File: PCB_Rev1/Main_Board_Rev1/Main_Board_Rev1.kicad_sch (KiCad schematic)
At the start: 0 parts

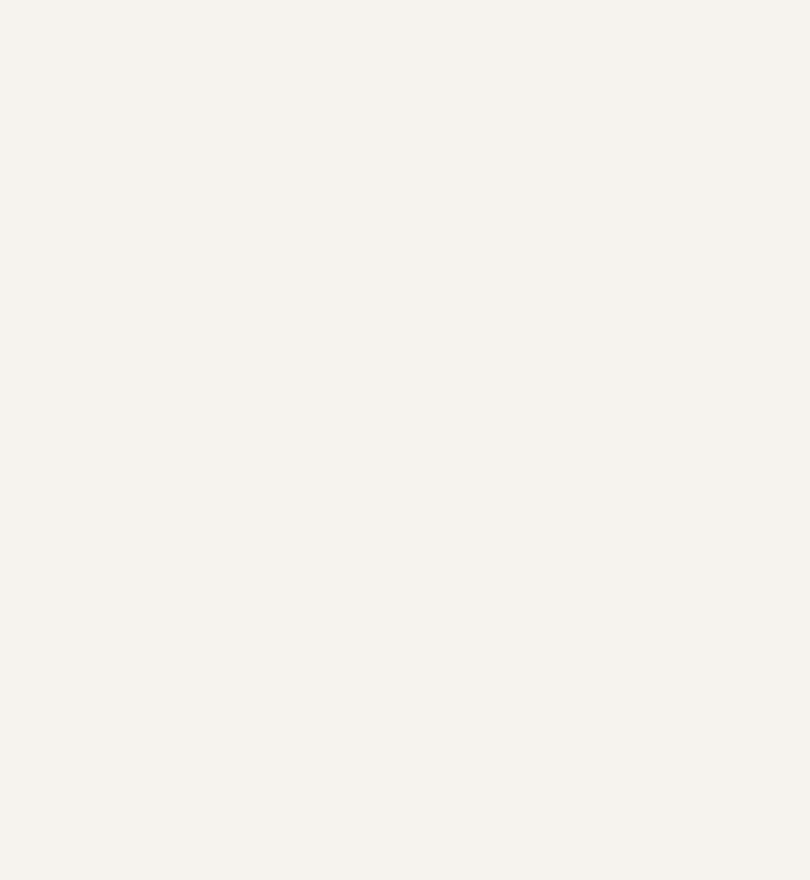
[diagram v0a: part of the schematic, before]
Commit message: Raspberry Pi Component Placed
Raspberry Pi component placed in Main Board schematic root page
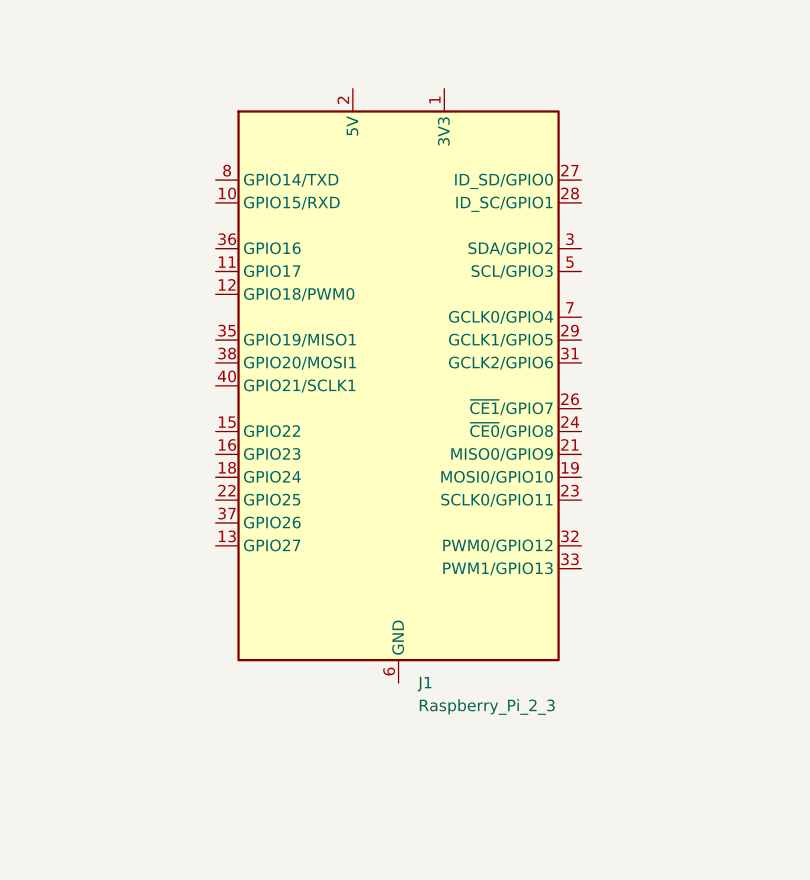
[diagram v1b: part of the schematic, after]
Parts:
- added J1: Raspberry_Pi_2_3, symbol Connector:Raspberry_Pi_2_3
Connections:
- new net: J1.1 (3V3), J1.17 (3V3)
- new net: J1.14 (GND), J1.20 (GND), J1.25 (GND), J1.30 (GND), J1.34 (GND), J1.39 (GND), J1.6 (GND), J1.9 (GND)
- new net: J1.2 (5V), J1.4 (5V)
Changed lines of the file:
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@@
 	(generator_version "8.0")
 	(paper "A4")
+	(symbol
+		(lib_id "Connector:Raspberry_Pi_2_3")
+		(at 140.97 64.77 0)
+		(unit 1)
+		(exclude_from_sim no)
+		(in_bom yes)
+		(on_board yes)
+		(dnp no)
+		(fields_autoplaced yes)
+		(property "Reference" "J1"
+			(at 143.1641 97.79 0)
+			(effects
+				(font
+					(size 1.27 1.27)
+				)
+				(justify left)
+			)
+		)
+		(property "Value" "Raspberry_Pi_2_3"
+			(at 143.1641 100.33 0)
+			(effects
+				(font
+					(size 1.27 1.27)
+				)
+				(justify left)
+			)
+		)
+		(property "Footprint" ""
+			(at 140.97 64.77 0)
+			(effects
+				(font
+					(size 1.27 1.27)
+				)
+				(hide yes)
+			)
+		)
+		(property "Datasheet" "https://www.raspberrypi.org/documentation/hardware/raspberrypi/schematics/rpi_SCH_3bplus_1p0_reduced.pdf"
+			(at 201.93 109.22 0)
+			(effects
+				(font
+					(size 1.27 1.27)
+				)
+				(hide yes)
+			)
+		)
+		(property "Description" "expansion header for Raspberry Pi 2 & 3"
+			(at 140.97 64.77 0)
+			(effects
+				(font
+					(size 1.27 1.27)
+				)
+				(hide yes)
+			)
+		)
+		(pin "34"
+		)
+		(pin "24"
+		)
+		(pin "28"
+		)
+		(pin "35"
+		)
+		(pin "37"
+		)
+		(pin "38"
+		)
+		(pin "1"
+		)
+		(pin "21"
+		)
+		(pin "3"
+		)
+		(pin "25"
+		)
+		(pin "10"
+		)
+		(pin "11"
+		)
+		(pin "19"
+		)
+		(pin "33"
+		)
+		(pin "39"
+		)
+		(pin "5"
+		)
+		(pin "32"
+		)
+		(pin "27"
+		)
+		(pin "18"
+		)
+		(pin "30"
+		)
+		(pin "26"
+		)
+		(pin "8"
+		)
+		(pin "17"
+		)
+		(pin "14"
+		)
+		(pin "15"
+		)
+		(pin "12"
+		)
+		(pin "16"
+		)
+		(pin "31"
+		)
+		(pin "36"
+		)
+		(pin "2"
+		)
+		(pin "29"
+		)
+		(pin "13"
+		)
+		(pin "20"
+		)
+		(pin "22"
+		)
+		(pin "4"
+		)
+		(pin "6"
+		)
+		(pin "40"
+		)
+		(pin "23"
+		)
+		(pin "7"
+		)
+		(pin "9"
+		)
+		(instances
+			(project ""
+				(path "/8f5a23de-a1fa-4202-92fb-c2ac3de0338c"
+					(reference "J1")
+					(unit 1)
+				)
+			)
+		)
+	)
 	(sheet
 		(at 21.59 105.41)

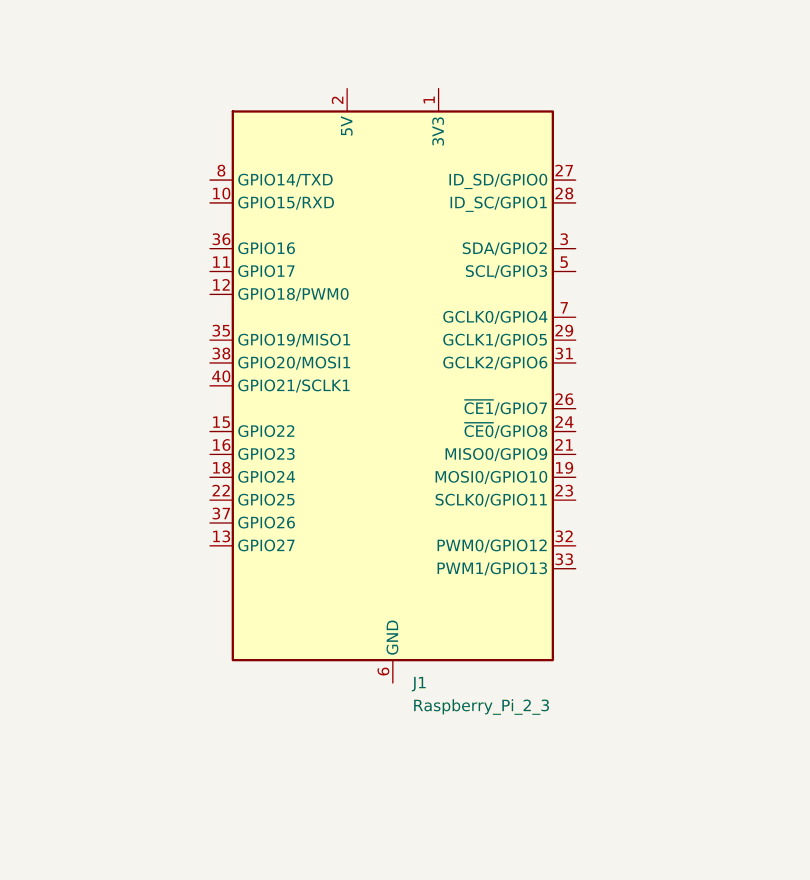
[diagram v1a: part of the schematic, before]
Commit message: Motor Drive Circuit
L298N motor driver and motor connections added
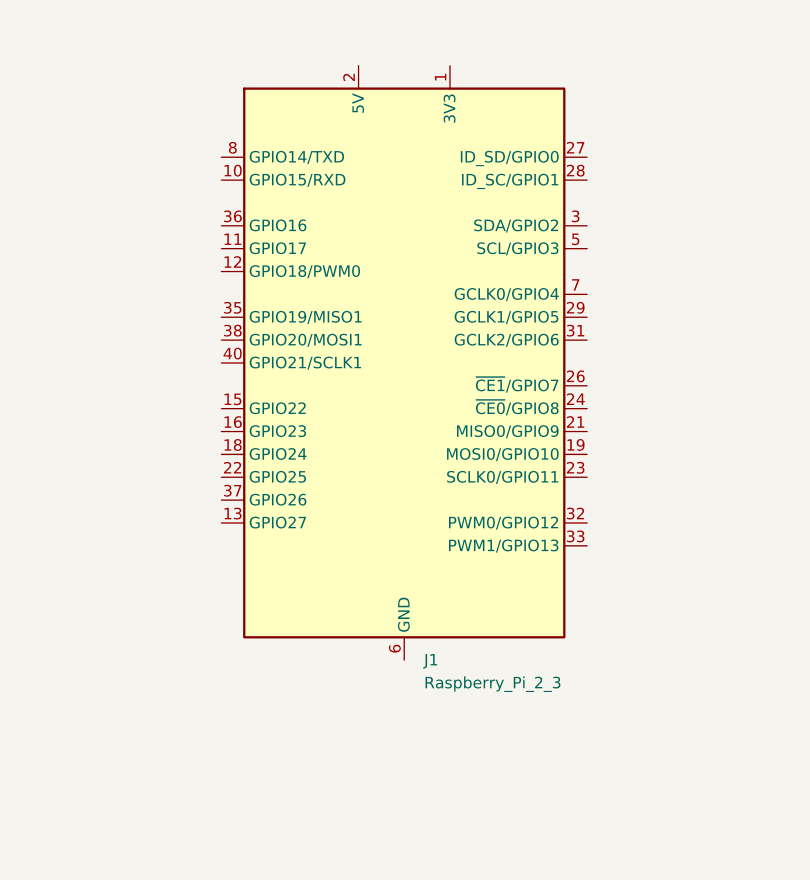
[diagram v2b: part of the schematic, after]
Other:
- moved on the sheet: J1
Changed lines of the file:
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@@
 	(symbol
 		(lib_id "Connector:Raspberry_Pi_2_3")
-		(at 140.97 64.77 0)
+		(at 142.24 62.23 0)
 		(unit 1)
 		(exclude_from_sim no)
@@
 		(fields_autoplaced yes)
 		(property "Reference" "J1"
-			(at 143.1641 97.79 0)
+			(at 144.4341 95.25 0)
 			(effects
 				(font
@@
 		)
 		(property "Value" "Raspberry_Pi_2_3"
-			(at 143.1641 100.33 0)
+			(at 144.4341 97.79 0)
 			(effects
 				(font
@@
 		)
 		(property "Footprint" ""
-			(at 140.97 64.77 0)
+			(at 142.24 62.23 0)
 			(effects
 				(font
@@
 		)
 		(property "Datasheet" "https://www.raspberrypi.org/documentation/hardware/raspberrypi/schematics/rpi_SCH_3bplus_1p0_reduced.pdf"
-			(at 201.93 109.22 0)
+			(at 203.2 106.68 0)
 			(effects
 				(font
@@
 		)
 		(property "Description" "expansion header for Raspberry Pi 2 & 3"
-			(at 140.97 64.77 0)
+			(at 142.24 62.23 0)
 			(effects
 				(font
